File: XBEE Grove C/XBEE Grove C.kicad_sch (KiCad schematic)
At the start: 38 parts, among them J12 TSW-102-07-G-S, J13 TSW-103-07-G-S, J2 B2B-PH-K-S, J3 USB_C_Receptacle_USB2.0_16P, Q1 SI2323DS-T1-E3, U1 FT232RL-REEL, U2 RT9167A-33GB

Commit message: Add files via upload
Corrected L1 and L2 footprints and uploaded boardview file for use with OpenBoardView.
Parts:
- L1, L2: footprint Inductor_SMD:L_0805_2012Metric -> Inductor_SMD:L_0603_1608Metric
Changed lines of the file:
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@@
       (effects (font (size 1.27 1.27)))
     )
-    (property "Footprint" "Inductor_SMD:L_0805_2012Metric" (at 35.56 111.76 0)
+    (property "Footprint" "Inductor_SMD:L_0603_1608Metric" (at 35.56 111.76 0)
       (effects (font (size 1.27 1.27)) hide)
     )
@@
       (effects (font (size 1.27 1.27)))
     )
-    (property "Footprint" "Inductor_SMD:L_0805_2012Metric" (at 55.88 69.215 0)
-      (effects (font (size 1.27 1.27)) hide)
-    )
+    (property "Footprint" "Inductor_SMD:L_0603_1608Metric" (at 55.88 69.215 0)
+      (effects (font (size 1.27 1.27)) hide)
+    )

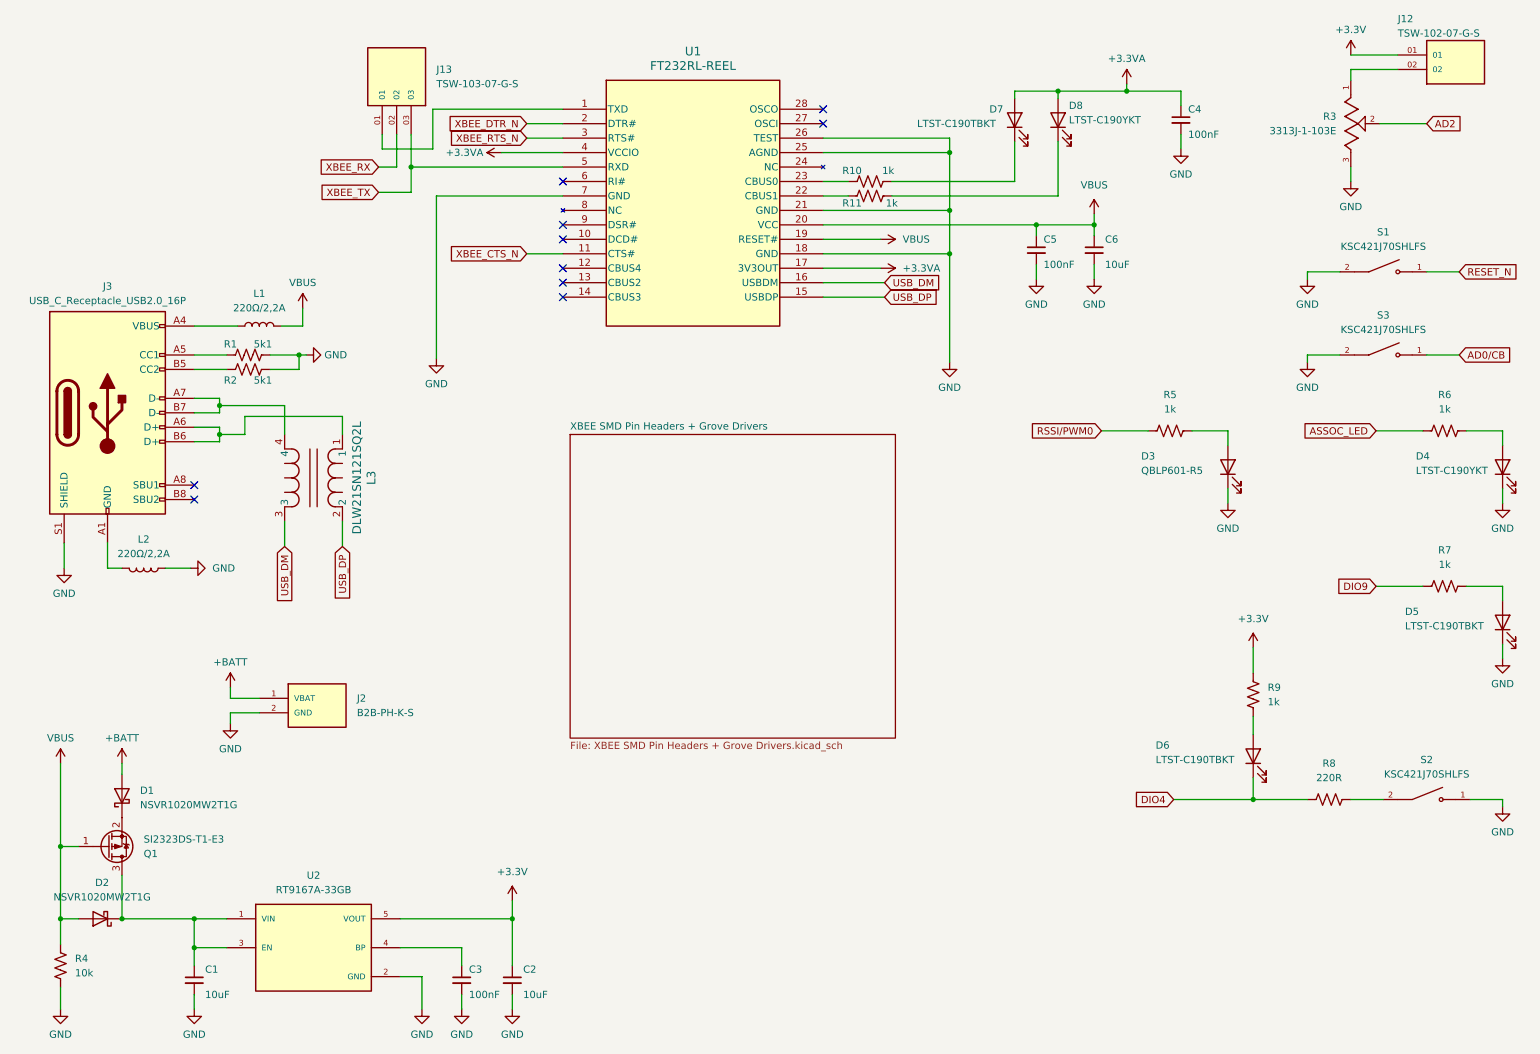
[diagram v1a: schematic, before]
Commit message: Add files via upload
Updated to v2 (all connectors now have the same number scheme as the original).
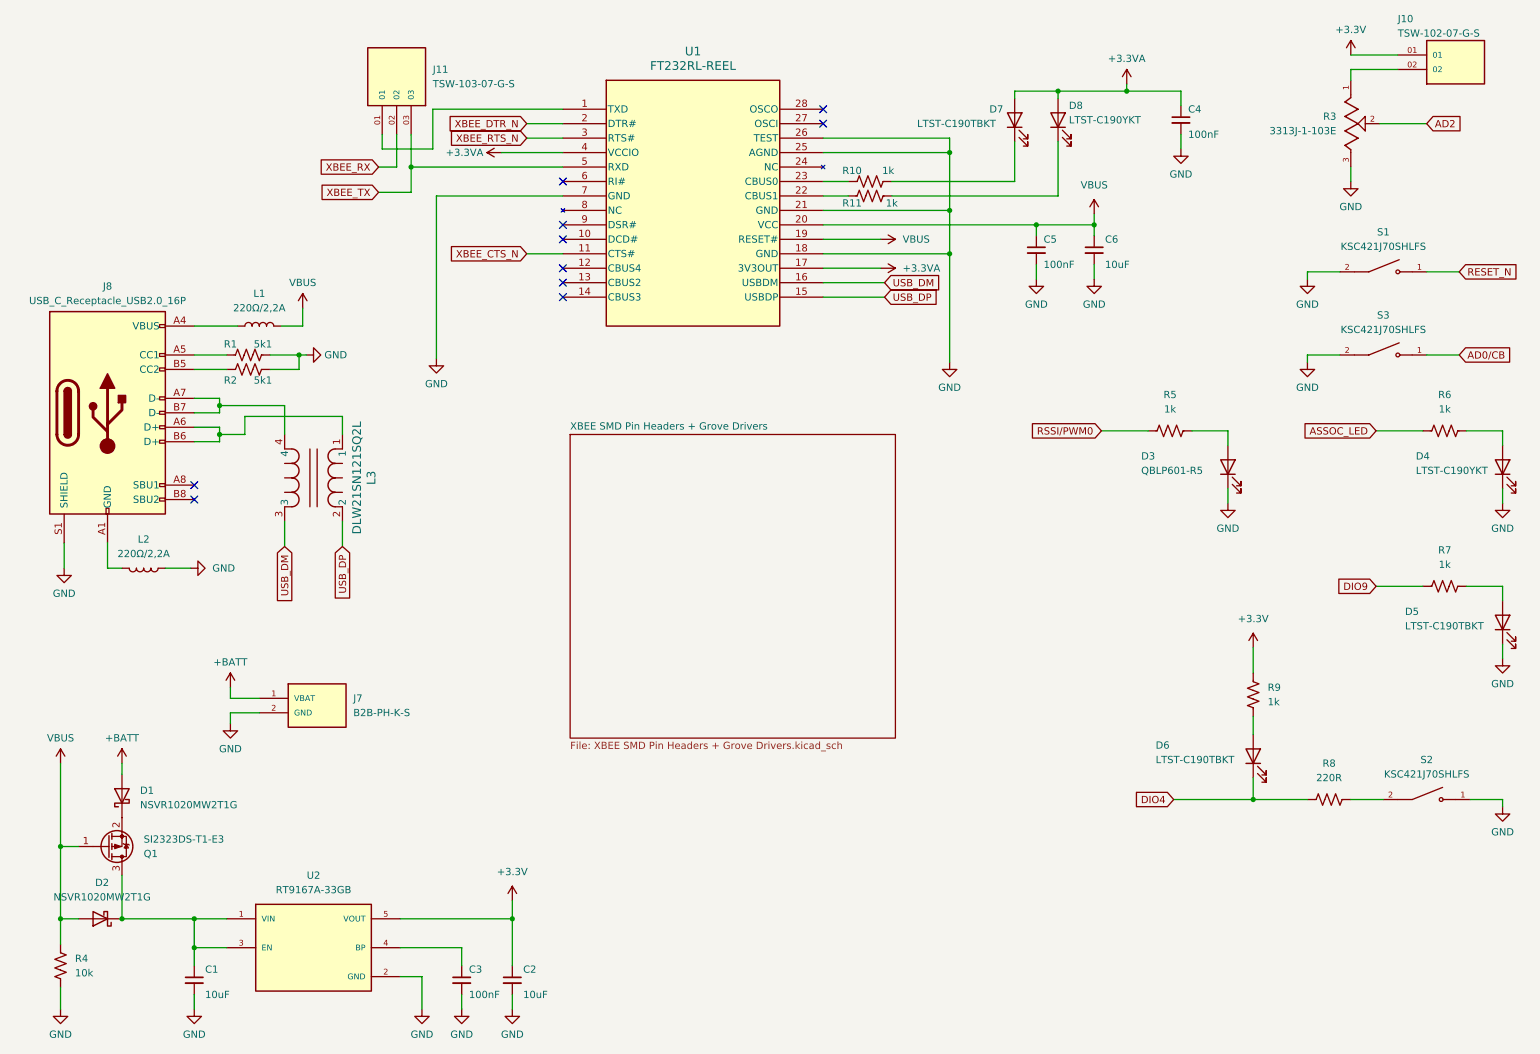
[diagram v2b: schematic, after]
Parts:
- renumbered J12 to J10, J13 to J11, J2 to J7, J3 to J8
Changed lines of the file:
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@@
   (symbol (lib_id "Connector:USB_C_Receptacle_USB2.0_16P") (at 29.21 84.455 0) (unit 1)
     (in_bom yes) (on_board yes) (dnp no) (fields_autoplaced)
-    (property "Reference" "J3" (at 29.21 62.23 0)
+    (property "Reference" "J8" (at 29.21 62.23 0)
       (effects (font (size 1.27 1.27)))
     )
@@
       (project "XBEE Grove C"
         (path "/c24e3a98-1eaf-47b8-85b4-f5ec44a15aa3"
-          (reference "J3") (unit 1)
+          (reference "J8") (unit 1)
         )
       )
@@
   (symbol (lib_id "XBEE_Grove_C:TSW-102-07-G-S") (at 266.065 24.13 0) (unit 1)
     (in_bom yes) (on_board yes) (dnp no)
-    (property "Reference" "J12" (at 255.905 15.24 0)
+    (property "Reference" "J10" (at 255.905 15.24 0)
       (effects (font (size 1.27 1.27)) (justify left))
     )
@@
       (project "XBEE Grove C"
         (path "/c24e3a98-1eaf-47b8-85b4-f5ec44a15aa3"
-          (reference "J12") (unit 1)
+          (reference "J10") (unit 1)
         )
       )
@@
   (symbol (lib_id "XBEE_Grove_C:B2B-PH-K-S") (at 66.04 137.16 0) (unit 1)
     (in_bom yes) (on_board yes) (dnp no) (fields_autoplaced)
-    (property "Reference" "J2" (at 73.025 134.62 0)
-      (effects (font (size 1.27 1.27)) (justify left))
-    )
-    (property "Value" "B2B-PH-K-S" (at 73.025 137.16 0)
+    (property "Reference" "J7" (at 72.39 134.62 0)
+      (effects (font (size 1.27 1.27)) (justify left))
+    )
+    (property "Value" "B2B-PH-K-S" (at 72.39 137.16 0)
       (effects (font (size 1.27 1.27)) (justify left))
     )
@@
       (project "XBEE Grove C"
         (path "/c24e3a98-1eaf-47b8-85b4-f5ec44a15aa3"
-          (reference "J2") (unit 1)
+          (reference "J7") (unit 1)
         )
       )
@@
   (symbol (lib_id "XBEE_Grove_C:TSW-103-07-G-S") (at 80.01 25.4 90) (unit 1)
     (in_bom yes) (on_board yes) (dnp no) (fields_autoplaced)
-    (property "Reference" "J13" (at 86.995 24.13 90)
+    (property "Reference" "J11" (at 86.36 24.13 90)
       (effects (font (size 1.27 1.27)) (justify right))
     )
-    (property "Value" "TSW-103-07-G-S" (at 86.995 26.67 90)
+    (property "Value" "TSW-103-07-G-S" (at 86.36 26.67 90)
       (effects (font (size 1.27 1.27)) (justify right))
     )
@@
       (project "XBEE Grove C"
         (path "/c24e3a98-1eaf-47b8-85b4-f5ec44a15aa3"
-          (reference "J13") (unit 1)
-        )
-      )
+          (reference "J11") (unit 1)
+        )
+      )

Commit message: Add files via upload
Updated schematic and boardview to match the original part numbers as best I could.
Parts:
- renumbered C4 to C10, C1 to C4, C3 to C5, C2 to C6, C6 to C7, C5 to C8, D3 to DS1, D4 to DS2, D5 to DS3, D7 to DS4, D8 to DS5, D6 to DS6, L3 to L2, L2 to L3, R4 to R1, R3 to R10, R5 to R11, R6 to R12, R7 to R13, R9 to R14, R8 to R15, R1 to R2, R2 to R3, R10 to R5, R11 to R6, S3 to S2, S2 to S3
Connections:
- net +3.3V: now also R14.2; no longer R14.1
- net at DS6.2 (A): now also R14.1; no longer R14.2
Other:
- moved on the sheet: C7, C8, R14
